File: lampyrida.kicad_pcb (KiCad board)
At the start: 2 copper layers, 66.2 x 39.2 mm, 15 parts, among them K1 SW_Push_45deg, K2 SW_Push_45deg, K3 SW_Push_45deg, K4 SW_Push_45deg, U1 RP2040 Zero, U2 TXB0101DBV

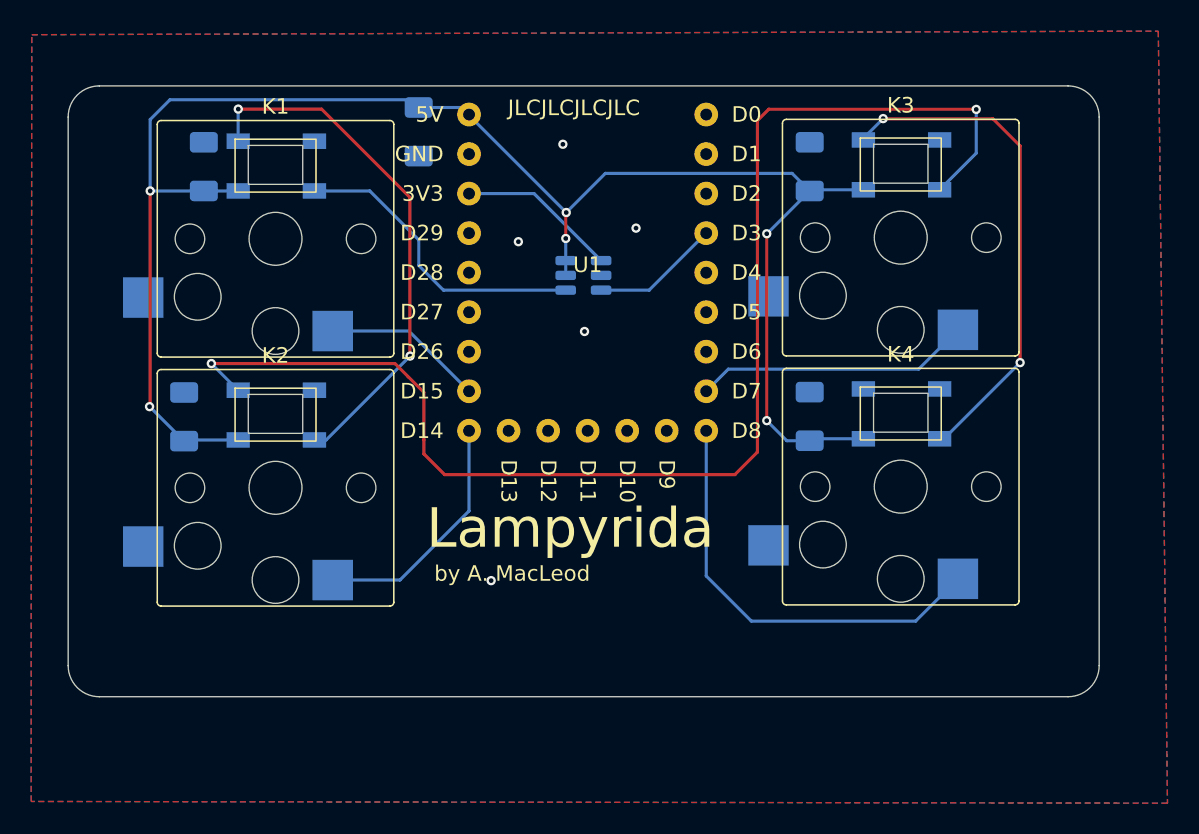
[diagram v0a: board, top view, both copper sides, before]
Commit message: Add R1, improve ground plane, add labels.
Fixes #7 by making more room for the ground pour to go around things
and with some better-placed vias.

Fixes #6 by adding labels, both in schematic and PCB, for capacitors
and the new resistor.

Fixes #5 by adding a spot for a 500-ish Ohm resistor on the LED data
input line.

Fixes #2 by moving C1 further away from the LED footprint.
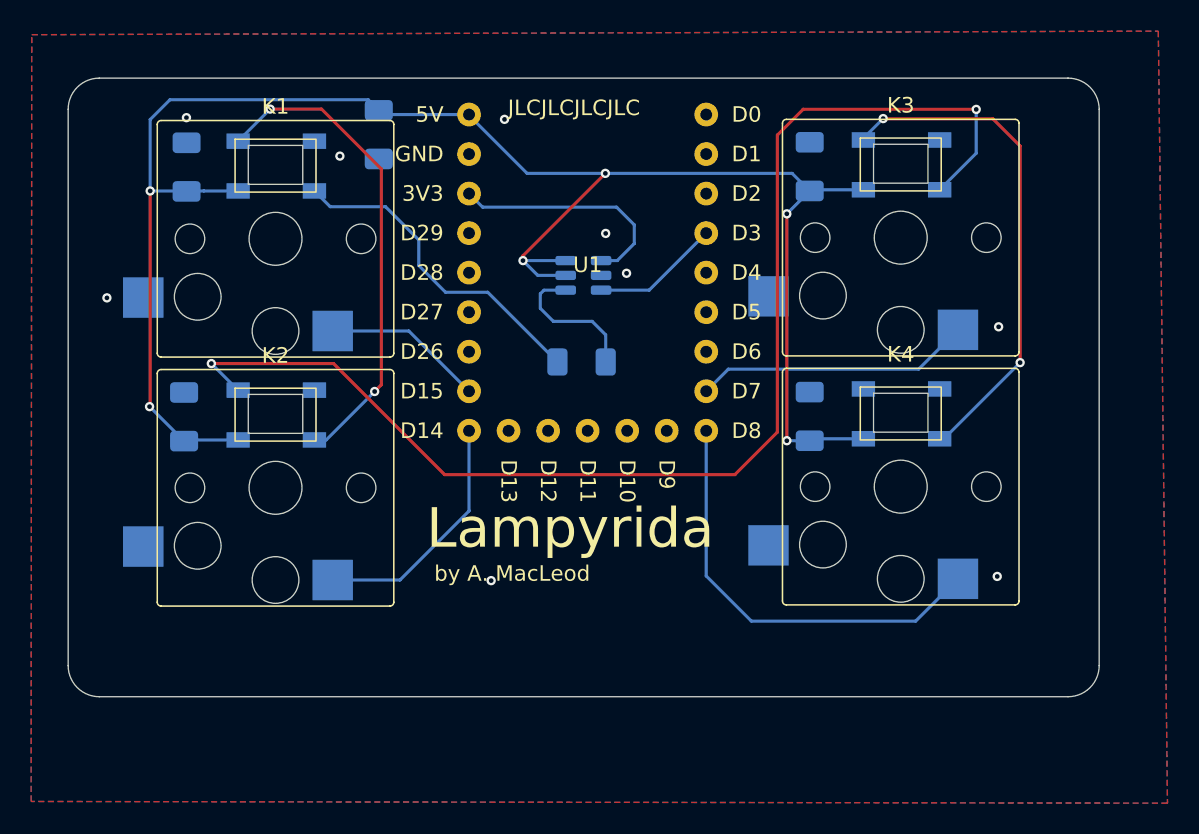
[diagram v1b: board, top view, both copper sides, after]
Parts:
- added R1: R, Resistor_SMD:R_1206_3216Metric_Pad1.30x1.75mm_HandSolder, B.Cu at (50.0, 38.0)
- moved C5 2.57 mm to (37.0, 23.4)
- moved C1 1.11 mm to (24.6, 25.5)
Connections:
- D1 pad 2: Net-(D1-DIN) -> /RGB5V
- U2 pad 4: Net-(D1-DIN) -> Net-(U2-B)
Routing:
- net /RGB5V: track 0.00 -> 21.1 mm
- net Net-(D1-DIN): track 19.7 -> 0.00 mm
- net Net-(U2-B): track 0.00 -> 9.31 mm
- net +5V: track 108.5 -> 115.0 mm
- net VCC: track 10.3 -> 15.2 mm
- net Net-(D2-DOUT): track 85.2 -> 81.6 mm
- net Net-(D1-DOUT): track 34.0 -> 31.3 mm
- net GND: vias 5 -> 9
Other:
- board size 66.2 x 39.2 mm -> 66.2 x 39.8 mm
- board text added: "0.1μF"
- board text added: "100~1000μF"
- board text added: "~500Ω"

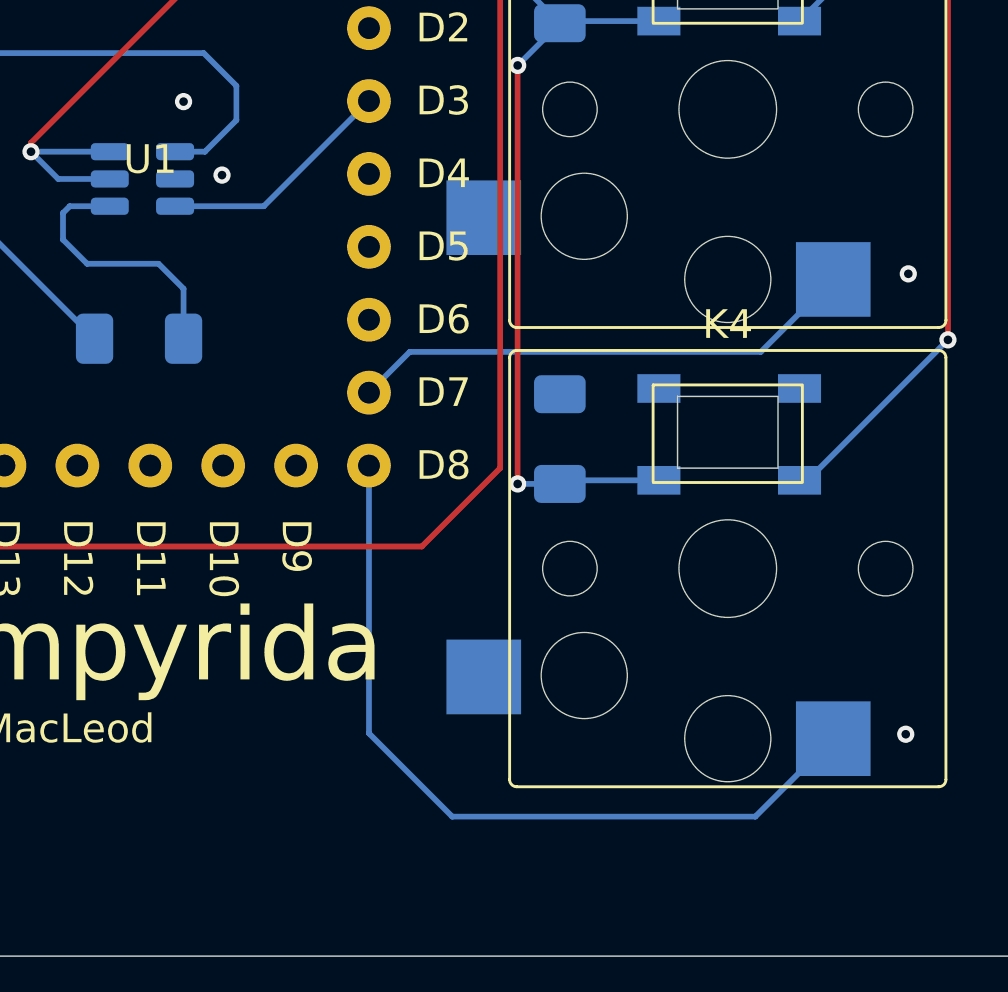
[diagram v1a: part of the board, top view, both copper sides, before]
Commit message: Fixes #4 by swapping which end of K3 and K4 is connected to ground.
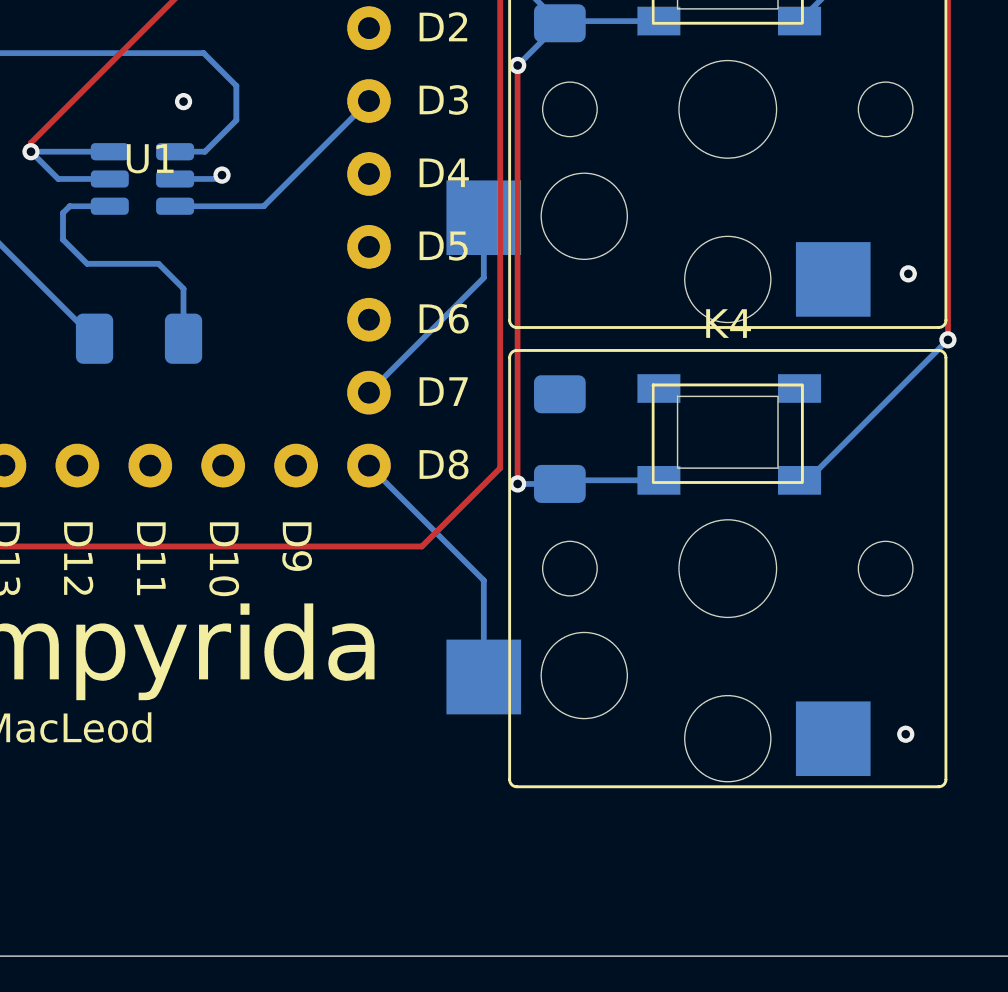
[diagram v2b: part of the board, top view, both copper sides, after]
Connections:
- K3 pad 1: key3 -> GND
- K3 pad 2: GND -> key3
- K4 pad 1: key4 -> GND
- K4 pad 2: GND -> key4
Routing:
- net key4: track 27.8 -> 9.02 mm
- net key3: track 17.8 -> 7.75 mm
- net GND: track 0.00 -> 1.69 mm
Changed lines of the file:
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@@
 			(size 2.6 2.6)
 			(layers "B.Cu" "B.Paste" "B.Mask")
-			(net 24 "key3")
+			(net 16 "GND")
 			(pinfunction "1")
 			(pintype "passive")
@@
 			(size 2.6 2.6)
 			(layers "B.Cu" "B.Paste" "B.Mask")
-			(net 16 "GND")
+			(net 24 "key3")
 			(pinfunction "2")
 			(pintype "passive")
@@
 			(size 2.6 2.6)
 			(layers "B.Cu" "B.Paste" "B.Mask")
-			(net 25 "key4")
+			(net 16 "GND")
 			(pinfunction "1")
 			(pintype "passive")
@@
 			(size 2.6 2.6)
 			(layers "B.Cu" "B.Paste" "B.Mask")
-			(net 16 "GND")
+			(net 25 "key4")
 			(pinfunction "2")
 			(pintype "passive")
@@
 		(effects
 			(font
-				(size 0.7 0.7)
+				(size 0.8 0.8)
 				(thickness 0.1)
 			)
@@
 		(effects
 			(font
-				(size 0.7 0.7)
+				(size 0.8 0.8)
 				(thickness 0.1)
 			)
@@
 		(effects
 			(font
-				(size 0.7 0.7)
+				(size 0.8 0.8)
 				(thickness 0.1)
 			)
@@
 		(effects
 			(font
-				(size 0.7 0.7)
+				(size 0.8 0.8)
 				(thickness 0.1)
 			)
@@
 		(effects
 			(font
-				(size 0.7 0.7)
+				(size 0.8 0.8)
 				(thickness 0.1)
 			)
@@
 	)
 	(gr_text "100~1000μF"
-		(at 36.97 23.38 90)
+		(at 37.04 24.23 90)
 		(layer "B.SilkS")
 		(effects
 			(font
-				(size 0.5 0.5)
+				(size 0.8 0.8)
 				(thickness 0.1)
 			)
@@
 	)
 	(segment
+		(start 52.745 32.425)
+		(end 52.88 32.29)
+		(width 0.2)
+		(layer "B.Cu")
+		(net 16)
+	)
+	(segment
+		(start 51.245 32.425)
+		(end 52.745 32.425)
+		(width 0.2)
+		(layer "B.Cu")
+		(net 16)
+	)
+	(segment
 		(start 46.225 31.475)
 		(end 46.225 31.165)
@@
 	)
 	(segment
-		(start 74.175 35.925)
-		(end 71.65 38.45)
-		(width 0.2)
-		(layer "B.Cu")
-		(net 24)
-	)
-	(segment
-		(start 59.42 38.45)
-		(end 58 39.87)
+		(start 58 39.87)
+		(end 62 35.87)
 		(width 0.2)
 		(layer "B.Cu")
@@
 	)
 	(segment
-		(start 71.65 38.45)
-		(end 59.42 38.45)
+		(start 62 35.87)
+		(end 62 33.775)
 		(width 0.2)
 		(layer "B.Cu")
@@
 	)
 	(segment
-		(start 71.46 54.64)
-		(end 74.175 51.925)
-		(width 0.2)
-		(layer "B.Cu")
-		(net 25)
-	)
-	(segment
-		(start 60.9 54.64)
-		(end 71.46 54.64)
-		(width 0.2)
-		(layer "B.Cu")
-		(net 25)
-	)
-	(segment
 		(start 58 42.41)
-		(end 58 51.74)
+		(end 62 46.41)
 		(width 0.2)
 		(layer "B.Cu")
@@
 	)
 	(segment
-		(start 58 51.74)
-		(end 60.9 54.64)
+		(start 62 46.41)
+		(end 62 49.775)
 		(width 0.2)
 		(layer "B.Cu")

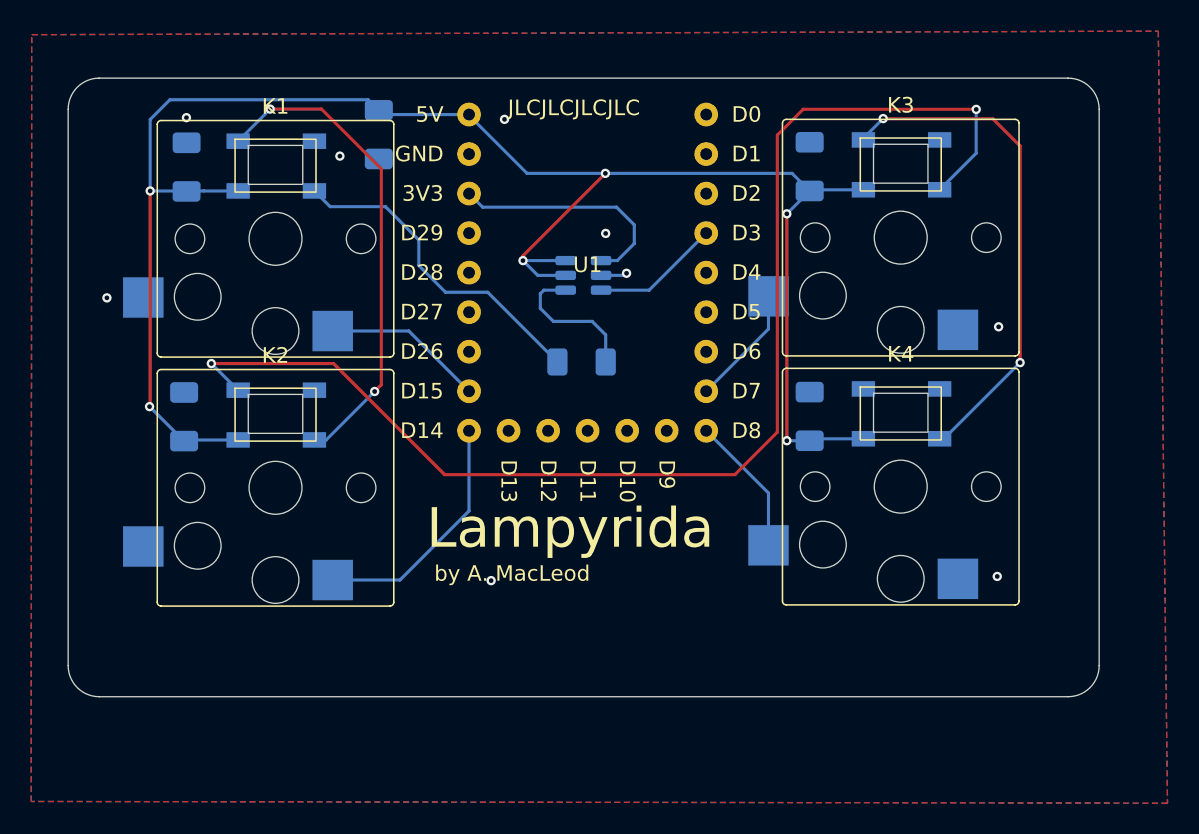
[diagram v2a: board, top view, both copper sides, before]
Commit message: Rerouting traces with new non-5V net.
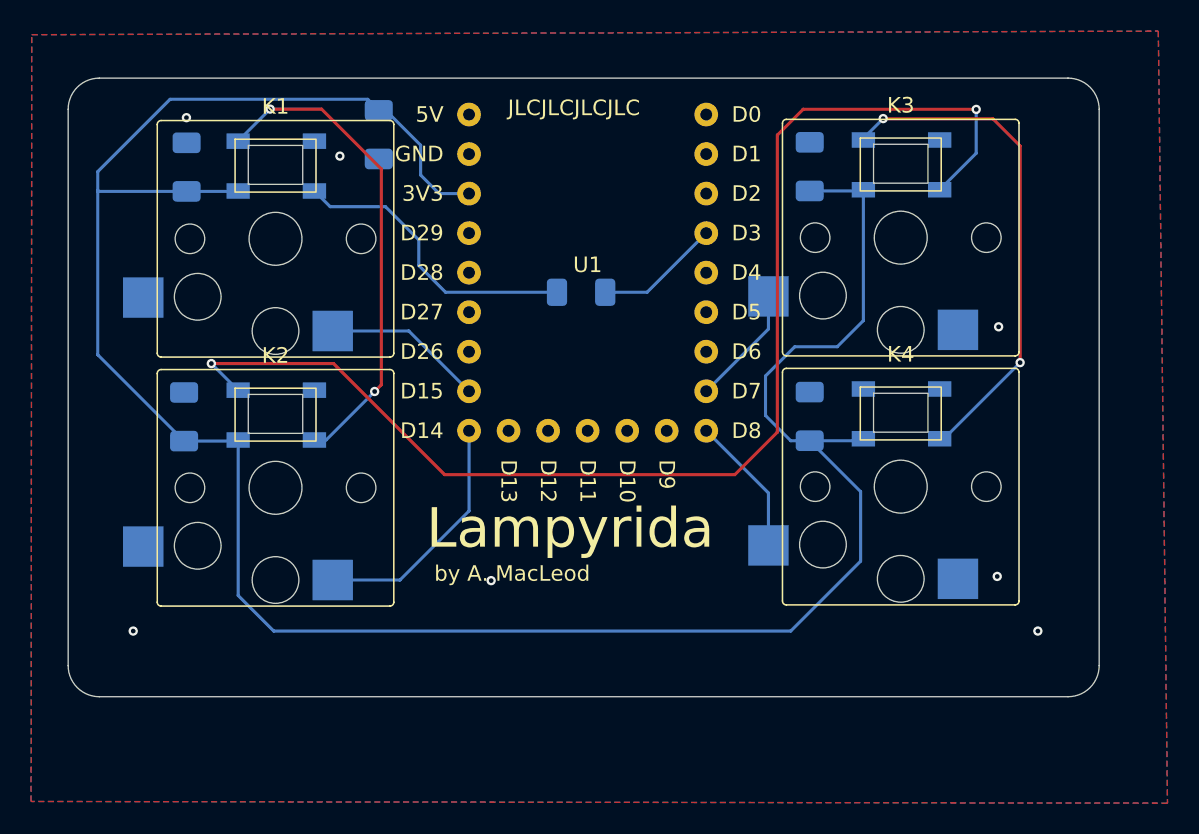
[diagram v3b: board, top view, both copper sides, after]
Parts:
- removed U2: TXB0101DBV, Package_TO_SOT_SMD:SOT-23-6
- moved R1 4.48 mm to (50.0, 33.5)
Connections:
- net /RGB5V renamed /RGB_Serial
- C1 pad 2: +5V -> VCC
- C2 pad 2: +5V -> VCC
- C3 pad 2: +5V -> VCC
- C4 pad 2: +5V -> VCC
- C5 pad 1: +5V -> VCC
- D1 pad 3: +5V -> VCC
- D2 pad 3: +5V -> VCC
- D3 pad 3: +5V -> VCC
- D4 pad 3: +5V -> VCC
- R1 pad 1: Net-(U2-B) -> RGB
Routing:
- net VCC: track 15.2 -> 152.8 mm
- net +5V: track 115.0 -> 0.00 mm, vias 6 -> 0
- net Net-(U2-B): track 9.31 -> 0.00 mm
- net /RGB_Serial: track 21.1 -> 19.2 mm
- net GND: track 1.69 -> 0.00 mm, vias 9 -> 7
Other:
- board text added: "(v0.0.2)"
- board text removed: "(v0.0.1)"

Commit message: Fixing SK6812-MiniE footprint and rerouting traces to match.
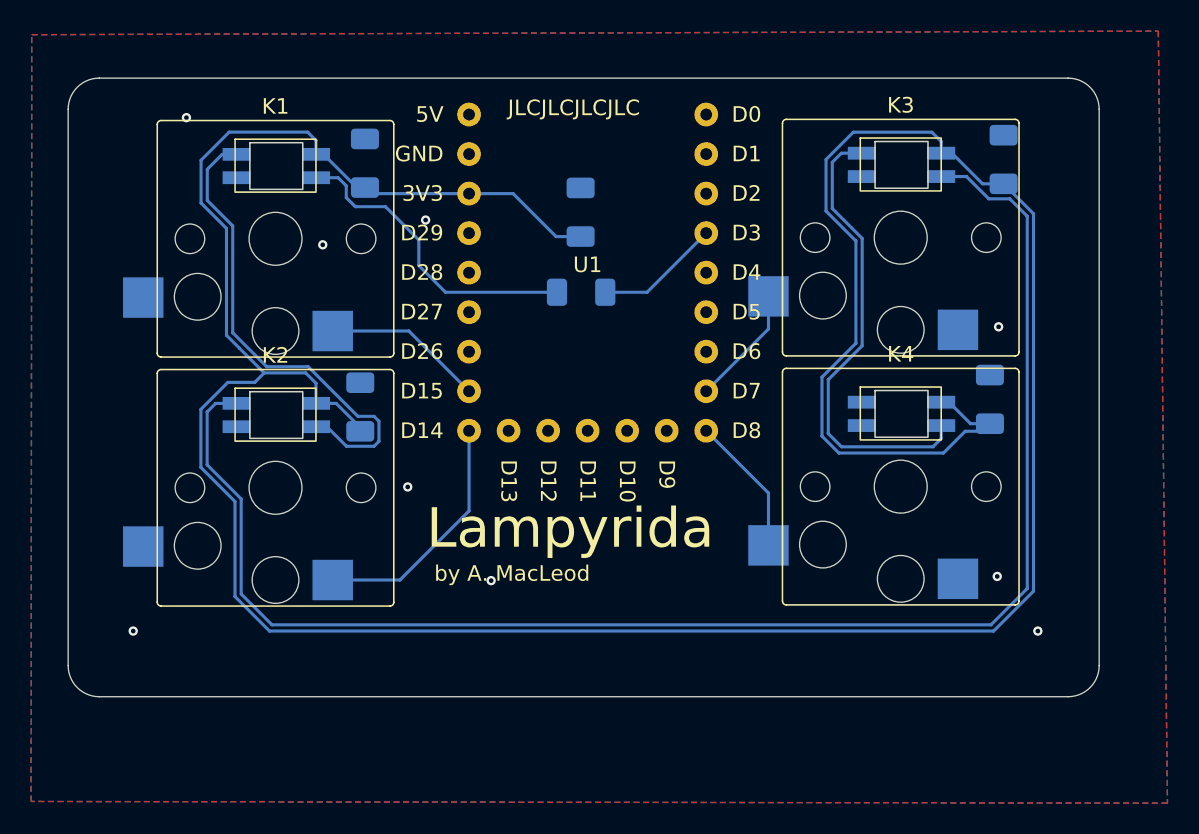
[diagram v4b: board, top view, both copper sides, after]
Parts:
- D1, D2, D3, D4: footprint LED_SMD:LED_SK6812_PLCC4_5.0x5.0mm_P3.2mm -> keyboard_parts:LED_RGB_SK6812Mini-E; moved to F.Cu
- moved C5 13.9 mm to (49.9, 28.4), turned to 90 degrees
- moved C3 12.5 mm to (77.1, 25.0)
- moved C4 11.6 mm to (76.2, 40.4)
- moved C1 11.5 mm to (36.1, 25.2)
- moved C2 11.3 mm to (35.8, 40.9)
- turned D1 to 0 degrees
- turned D2 to 0 degrees
- turned D3 to 0 degrees
- turned D4 to 0 degrees
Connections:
- D1 pad 1: GND -> Net-(D1-VSS)
- D1 pad 2: /RGB_Serial -> GND
- D1 pad 3: VCC -> /RGB_Serial
- D1 pad 4: Net-(D1-DOUT) -> VCC
- D2 pad 1: GND -> Net-(D2-VSS)
- D2 pad 2: Net-(D1-DOUT) -> GND
- D2 pad 3: VCC -> Net-(D1-VSS)
- D2 pad 4: Net-(D2-DOUT) -> VCC
- D3 pad 1: GND -> Net-(D3-VSS)
- D3 pad 2: Net-(D2-DOUT) -> GND
- D3 pad 3: VCC -> Net-(D2-VSS)
- D3 pad 4: Net-(D3-DOUT) -> VCC
- D4 pad 1: GND -> unconnected-(D4-DOUT-Pad1)
- D4 pad 2: Net-(D3-DOUT) -> GND
- D4 pad 3: VCC -> Net-(D3-VSS)
- D4 pad 4: unconnected-(D4-DOUT-Pad4) -> VCC
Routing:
- net Net-(D2-VSS): track 0.00 -> 97.5 mm
- net Net-(D2-DOUT): track 81.6 -> 0.00 mm, vias 2 -> 0
- net VCC: track 152.8 -> 200.1 mm
- net Net-(D3-DOUT): track 32.5 -> 0.00 mm, vias 2 -> 0
- net Net-(D1-DOUT): track 31.3 -> 0.00 mm, vias 2 -> 0
- net Net-(D1-VSS): track 0.00 -> 31.2 mm
- net Net-(D3-VSS): track 0.00 -> 29.9 mm
- net /RGB_Serial: track 19.2 -> 19.9 mm
- net GND: vias 7 -> 9

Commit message: Correcting DRC violations.
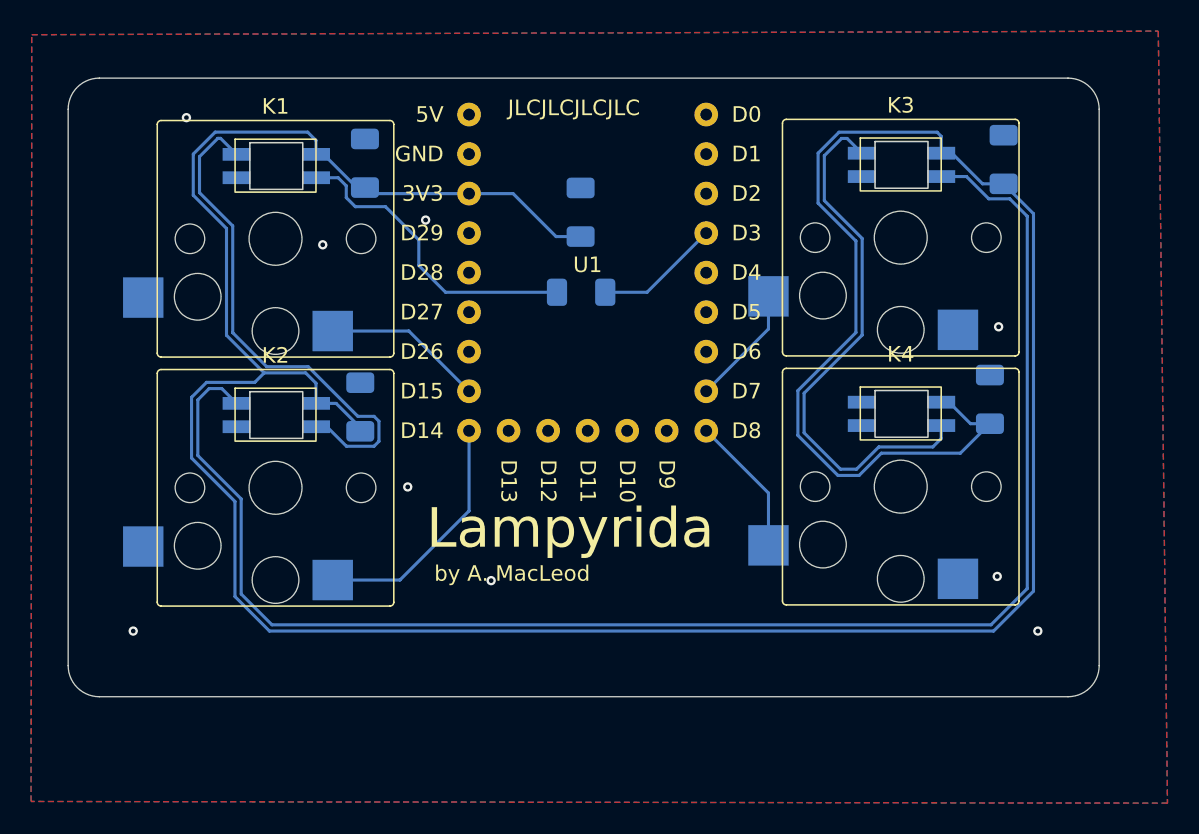
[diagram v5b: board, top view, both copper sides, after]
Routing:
- net VCC: track 200.1 -> 206.8 mm
- net Net-(D3-VSS): track 29.9 -> 35.0 mm
- net Net-(D2-VSS): track 97.5 -> 99.6 mm
- net Net-(D1-VSS): track 31.2 -> 33.2 mm
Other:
- board text added: "(v0.0.3)"
- board text removed: "(v0.0.2)"
